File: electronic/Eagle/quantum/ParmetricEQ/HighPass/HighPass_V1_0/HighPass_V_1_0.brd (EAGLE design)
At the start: 81.3 x 22.9 mm, 62 parts, among them IC1 OP275_SOIC8, IC2 OP275_SOIC8, IC3 OP275_SOIC8, IC4 TL072, IC5 TL072, U1 THAT2181SO8-US, U2 THAT2181SO8-US, U3 THAT2181SO8-US

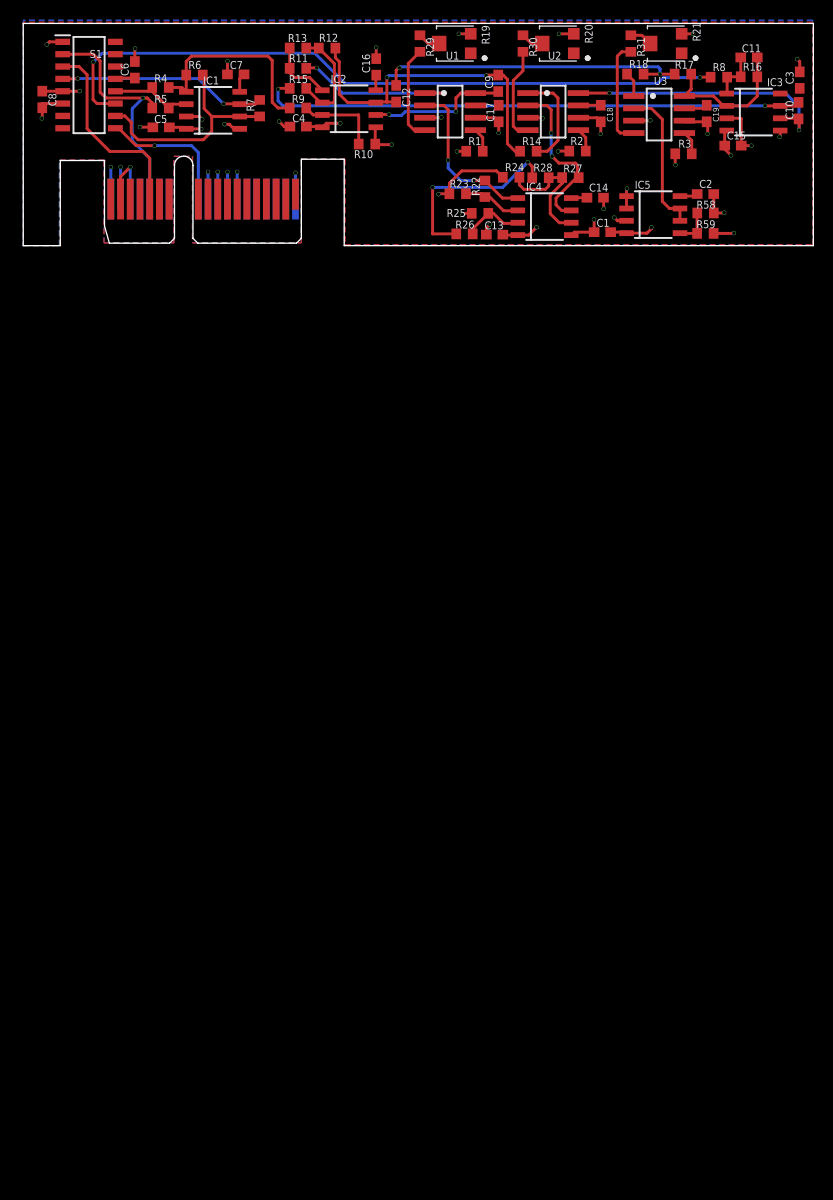
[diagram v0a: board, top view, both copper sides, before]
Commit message: finished EncoderPCB, Implemented Float OSC
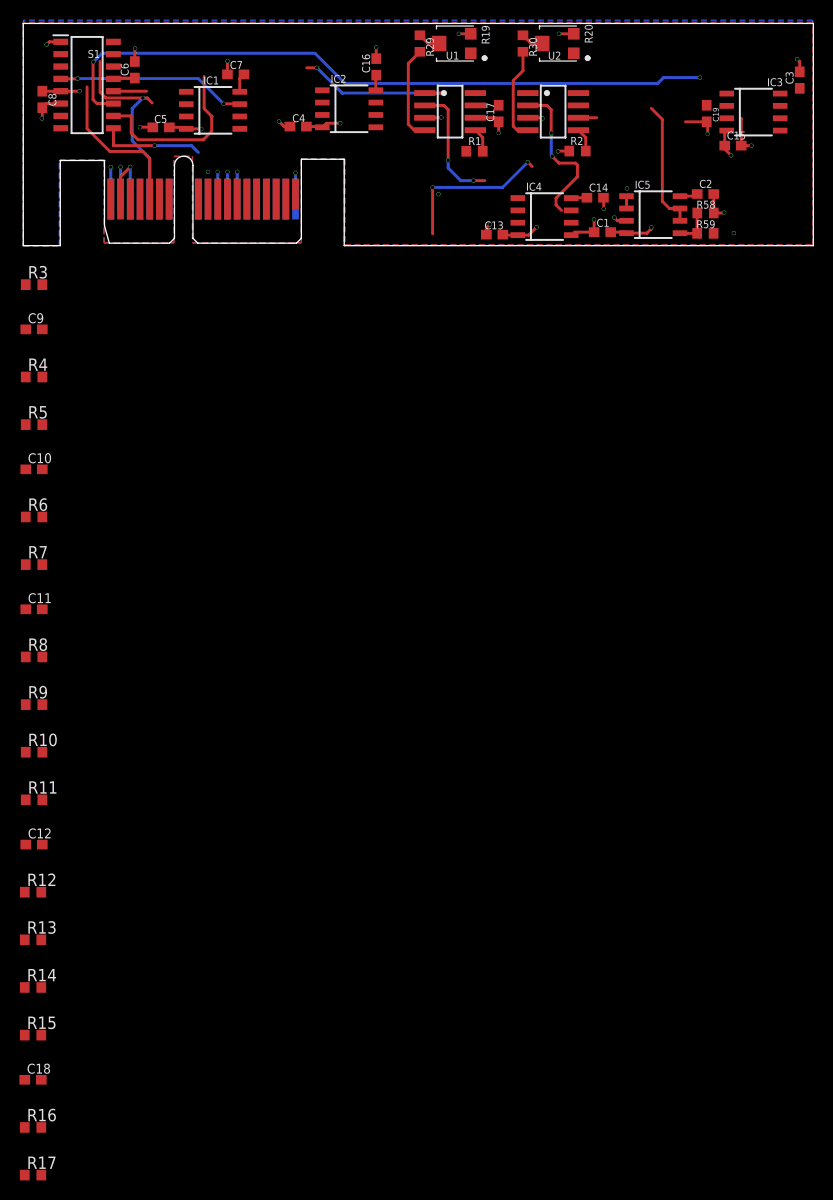
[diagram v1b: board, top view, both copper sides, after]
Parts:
- removed R18, R22, R23, R24, R25, R26, R27, R28: (no value), passive components:R0603
- removed R21: 50 k, electro_mechanical:TC33X2503G
- removed R31: 130 k, passive components:R0603
- removed U3: THAT2181SO8-US, THAT_Library:SO08
- C10, C11, C12, C9: value (none) -> 100 nF
- R10, R11, R12, R13, R14, R15, R4, R5, R6, R7, R8, R9: value (none) -> 130 k
- R16: value (none) -> 10 k
- R17: value (none) -> 56 k
- R3: value 5k1 -> 130 k
- moved R17 131.5 mm to (1.00, -95.5), turned to 0 degrees
- moved R16 130.8 mm to (1.00, -90.6)
- moved C18 115.3 mm to (1.00, -85.7), turned to 0 degrees
- moved R15 101.1 mm to (1.00, -81.1), turned to 0 degrees
- moved R14 100.0 mm to (1.00, -76.2)
- moved R13 96.6 mm to (1.00, -71.3)
- moved C11 92.9 mm to (1.10, -37.3)
- moved R8 92.3 mm to (1.10, -42.2)
- moved R12 91.0 mm to (1.00, -66.4), turned to 0 degrees
- moved C10 86.9 mm to (1.10, -22.9), turned to 0 degrees
- moved C12 85.8 mm to (1.10, -61.5), turned to 0 degrees
- moved R11 80.0 mm to (1.10, -56.9)
- moved R10 71.3 mm to (1.10, -52.0), turned to 0 degrees
- moved R3 68.2 mm to (1.10, -3.90)
- moved R9 67.1 mm to (1.10, -47.1)
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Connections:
- net BUFFERED_DAC4_BYPASS renamed BUFFERED_DAC4
- net DAC1_GAIN renamed DAC1_HIGHPASS_FREQ
- net DAC4_BYPASS renamed DAC4
- removed net AUDIO_PROCESSED: IC1.7, R7.2, S1.4
- removed net DAC2_FREQ: PCIE1.B8, R23.1, R24.1
- removed net DAC3_Q: PCIE1.B9, R26.2, R28.1
- removed net DIG_BOOST/CUT: PCIE1.B11, S1.9
- removed net E+_VCA3: IC5.6, IC5.7, U3.2
- removed net MID_BOOST: IC1.6, R6.2, R7.1, S1.10
- removed net MID_CUT: IC1.2, R4.1, R5.2, S1.12
- removed net MID_SIGNAL: R8.1, S1.11
- removed net N$10: C12.2, C9.2, IC2.7, R13.2, R14.1
- removed net N$12: C10.1, IC3.6, U2.8
- removed net N$14: C10.2, IC3.7, R15.2
- removed net N$15: C11.2, IC3.2, R16.2, R17.1, U3.8
- removed net N$18: IC4.2, R22.1, R23.2
- removed net N$19: IC4.3, R25.2, R26.1
- removed net N$21: IC4.6, R24.2, R27.1, R28.2
- removed net N$24: R21.2, R31.1
- removed net SYM_VCA3: R31.2, U3.4
- new net BUFFERED_DAC3: IC4.6, IC4.7, S1.9
- new net DAC1_HIGHSHELF_GAIN: PCIE1.B8, R17.2
- new net DAC3: IC4.5, PCIE1.B9
- new net DIG: PCIE1.B11
- new net HIGH_PASS_IN: R14.1, S1.4
- new net HIGH_PASS_OUT: IC2.1, R12.1, R13.2, S1.11
- new net LOW_SHELF_IN: R11.1, R8.1, S1.12
- new net LOW_SHELF_OUT: C11.1, C11.2, IC1.7, R6.2, R7.1, R7.2, R9.2
- net AUDIO_IN: now also S1.3; no longer R5.1, S1.2
- net AUDIO_OUT: now also S1.10, S1.2; no longer S1.3
- net E+_VCA1: now also IC4.2; no longer R22.2
- net E+_VCA2: now also IC5.6, IC5.7; no longer IC4.7, R27.2
- net GND: now also IC2.3, R16.1; no longer C18.2, IC3.3, IC3.5, IC4.5, R10.1, R25.1, U3.3, U3.6
- net N$11: now also C12.1, R10.1, R11.2; no longer R14.2, U2.1
- net N$13: now also IC2.2, R13.1, R14.2, R15.1; no longer C11.1, IC3.1, R16.1, R8.2
- net N$16: now also C18.2, IC2.7, R15.2; no longer R18.1, U3.1
- net N$17: now also C18.1, IC2.6, U2.8; no longer C12.1, R17.2, R18.2
- net N$3: now also C9.1, IC1.2, R3.1, U1.8; no longer R3.2, U3.5
- net N$4: now also C10.2, IC1.6, R4.2, R6.1, R8.2; no longer IC2.3, R10.2, R9.2
- net N$5: now also C9.2, R3.2, R4.1, R5.1; no longer R4.2, R6.1, R9.1
- net N$6: now also C10.1, R5.2; no longer IC2.2, R12.1, R13.1, R15.1
- net N$7: now also U2.1; no longer IC2.1, R11.1
- net N$8: now also C12.2, R10.2, R9.1; no longer R11.2
- net N$9: now also IC4.3, R16.2, R17.1; no longer C9.1, IC2.6, U1.8
- net V+: no longer C18.1, R21.1, U3.7
- net V-: no longer R21.3, R3.1
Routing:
- net MID_SIGNAL: track 71.8 -> 0.00 mm, vias 2 -> 0
- net HIGH_PASS_OUT: track 0.00 -> 70.5 mm, vias 0 -> 2
- net N$14: track 56.4 -> 0.00 mm, vias 2 -> 0
- net DAC3_Q: track 50.9 -> 0.00 mm, vias 3 -> 0
- net DAC3: track 0.00 -> 47.3 mm, vias 0 -> 3
- net DAC2_FREQ: track 38.6 -> 0.00 mm, vias 2 -> 0
- net N$10: track 34.7 -> 0.00 mm, vias 2 -> 0
- net N$17: track 32.7 -> 0.00 mm, vias 2 -> 0
- net DAC1_HIGHSHELF_GAIN: track 0.00 -> 30.1 mm, vias 0 -> 2
- net N$12: track 28.8 -> 0.00 mm, vias 2 -> 0
- net MID_BOOST: track 23.0 -> 0.00 mm
- net AUDIO_PROCESSED: track 21.5 -> 0.00 mm, vias 2 -> 0
- net N$5: track 20.7 -> 0.00 mm
- net HIGH_PASS_IN: track 0.00 -> 19.5 mm, vias 0 -> 2
- net E+_VCA3: track 15.2 -> 0.00 mm
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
